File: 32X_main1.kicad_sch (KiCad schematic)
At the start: 27 parts, among them IC504 315-5818, IC505 315-5805, IC509 74AC04

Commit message: Added LCSC Part # for some of the bird seed
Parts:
- C5: LCSC Part # (none) -> C2237864
- C5: LCSC Part # (none) -> C2182015
- FB7: LCSC Part # (none) -> C91037
- R561: LCSC Part # (none) -> C844640
- R562: LCSC Part # (none) -> C2077049
- R566: LCSC Part # (none) -> C2077067
- RM3, RM4, RM5, RM6: LCSC Part # (none) -> C110924
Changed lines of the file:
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@@
+      (effects (font (size 1.27 1.27)) hide)
+    )
+    (property "LCSC Part #" "C2077067" (at 49.53 125.73 0)
       (effects (font (size 1.27 1.27)) hide)
     )
@@
     )
     (property "DigiKey" "" (at 77.47 247.65 0)
+      (effects (font (size 1.27 1.27)) hide)
+    )
+    (property "LCSC Part #" "" (at 77.47 247.65 0)
       (effects (font (size 1.27 1.27)) hide)
     )
@@
       (effects (font (size 1.27 1.27)) hide)
     )
+    (property "LCSC Part #" "C2237864" (at 195.58 243.84 0)
+      (effects (font (size 1.27 1.27)) hide)
+    )
     (pin "1")
     (pin "2")
@@
     )
     (property "DigiKey" "" (at 278.13 244.475 0)
+      (effects (font (size 1.27 1.27)) hide)
+    )
+    (property "LCSC Part #" "" (at 278.13 244.475 0)
       (effects (font (size 1.27 1.27)) hide)
     )
@@
       (effects (font (size 1.27 1.27)) hide)
     )
+    (property "LCSC Part #" "C2237864" (at 194.945 183.515 0)
+      (effects (font (size 1.27 1.27)) hide)
+    )
     (pin "1")
     (pin "2")
@@
     )
     (property "DigiKey" "" (at 85.725 65.405 0)
+      (effects (font (size 1.27 1.27)) hide)
+    )
+    (property "LCSC Part #" "C110924" (at 85.725 65.405 0)
       (effects (font (size 1.27 1.27)) hide)
     )
@@
       (effects (font (size 1.27 1.27)) hide)
     )
+    (property "LCSC Part #" "C2182015" (at 207.645 243.84 0)
+      (effects (font (size 1.27 1.27)) hide)
+    )
     (pin "1")
     (pin "2")
@@
       (effects (font (size 1.27 1.27)) hide)
     )
+    (property "LCSC Part #" "C2182015" (at 291.465 161.29 0)
+      (effects (font (size 1.27 1.27)) hide)
+    )
     (pin "1")
     (pin "2")
@@
       (effects (font (size 1.27 1.27)) hide)
     )
+    (property "LCSC Part #" "C2237864" (at 272.415 161.29 0)
+      (effects (font (size 1.27 1.27)) hide)
+    )
     (pin "1")
     (pin "2")
@@
       (effects (font (size 1.27 1.27)) hide)
     )
+    (property "LCSC Part #" "C2237864" (at 282.575 161.29 0)
+      (effects (font (size 1.27 1.27)) hide)
+    )
     (pin "1")
     (pin "2")
@@
       (effects (font (size 1.27 1.27)) hide)
     )
+    (property "LCSC Part #" "" (at 108.585 198.755 0)
+      (effects (font (size 1.27 1.27)) hide)
+    )
     (pin "1")
     (pin "2")
@@
       (effects (font (size 1.27 1.27)) hide)
     )
+    (property "LCSC Part #" "" (at 263.525 203.2 0)
+      (effects (font (size 1.27 1.27)) hide)
+    )
     (pin "1")
     (pin "2")
@@
       (effects (font (size 1.27 1.27)) hide)
     )
+    (property "LCSC Part #" "" (at 118.11 184.785 0)
+      (effects (font (size 1.27 1.27)) hide)
+    )
     (pin "1")
     (pin "2")
@@
       (effects (font (size 1.27 1.27)) hide)
     )
+    (property "LCSC Part #" "" (at 232.41 243.84 0)
+      (effects (font (size 1.27 1.27)) hide)
+    )
     (pin "1")
     (pin "2")
@@
       (effects (font (size 1.27 1.27)) hide)
     )
+    (property "LCSC Part #" "C91037" (at 236.22 203.2 0)
+      (effects (font (size 1.27 1.27)) hide)
+    )
     (pin "1")
     (pin "2")
@@
       (effects (font (size 1.27 1.27)) hide)
     )
+    (property "LCSC Part #" "C91037" (at 153.67 169.545 0)
+      (effects (font (size 1.27 1.27)) hide)
+    )
     (pin "1")
     (pin "2")
@@
     )
     (property "DigiKey" "" (at 98.425 247.65 0)
+      (effects (font (size 1.27 1.27)) hide)
+    )
+    (property "LCSC Part #" "" (at 98.425 247.65 0)
       (effects (font (size 1.27 1.27)) hide)
     )
@@
       (effects (font (size 1.27 1.27)) hide)
     )
+    (property "LCSC Part #" "C110924" (at 85.725 104.14 0)
+      (effects (font (size 1.27 1.27)) hide)
+    )
     (pin "1")
     (pin "2")
@@
     )
     (property "DigiKey" "" (at 118.11 156.845 0)
+      (effects (font (size 1.27 1.27)) hide)
+    )
+    (property "LCSC Part #" "" (at 118.11 156.845 0)
       (effects (font (size 1.27 1.27)) hide)
     )
@@
       (effects (font (size 1.27 1.27)) hide)
     )
+    (property "LCSC Part #" "C844640" (at 88.265 234.315 0)
+      (effects (font (size 1.27 1.27)) hide)
+    )
     (pin "1")
     (pin "2")
@@
     )
     (property "DigiKey" "" (at 85.725 84.455 0)
+      (effects (font (size 1.27 1.27)) hide)
+    )
+    (property "LCSC Part #" "C110924" (at 85.725 84.455 0)
       (effects (font (size 1.27 1.27)) hide)
     )
@@
       (effects (font (size 1.27 1.27)) hide)
     )
+    (property "LCSC Part #" "C2077049" (at 59.055 247.65 0)
+      (effects (font (size 1.27 1.27)) hide)
+    )
     (pin "1")
     (pin "2")
@@
       (effects (font (size 1.27 1.27)) hide)
     )
+    (property "LCSC Part #" "" (at 203.835 170.815 0)
+      (effects (font (size 1.27 1.27)) hide)
+    )
     (pin "1")
     (pin "2")
@@
     )
     (property "DigiKey" "" (at 220.345 243.84 0)
+      (effects (font (size 1.27 1.27)) hide)
+    )
+    (property "LCSC Part #" "C2182015" (at 220.345 243.84 0)
       (effects (font (size 1.27 1.27)) hide)
     )
@@
     )
     (property "DigiKey" "" (at 249.555 48.26 0)
+      (effects (font (size 1.27 1.27)) hide)
+    )
+    (property "LCSC Part #" "" (at 249.555 48.26 0)
       (effects (font (size 1.27 1.27)) hide)
     )
@@
       (effects (font (size 1.27 1.27)) hide)
     )
+    (property "LCSC Part #" "C2182015" (at 203.835 183.515 0)
+      (effects (font (size 1.27 1.27)) hide)
+    )
     (pin "1")
     (pin "2")
@@
     )
     (property "DigiKey" "" (at 249.555 203.2 0)
+      (effects (font (size 1.27 1.27)) hide)
+    )
+    (property "LCSC Part #" "" (at 249.555 203.2 0)
       (effects (font (size 1.27 1.27)) hide)
     )
@@
       (effects (font (size 1.27 1.27)) hide)
     )
+    (property "LCSC Part #" "" (at 153.67 179.705 0)
+      (effects (font (size 1.27 1.27)) hide)
+    )
     (pin "1")
     (pin "2")
@@
       (effects (font (size 1.27 1.27)) hide)
     )
+    (property "LCSC Part #" "" (at 132.715 156.845 0)
+      (effects (font (size 1.27 1.27)) hide)
+    )
     (pin "1")
     (pin "2")
@@
     )
     (property "DigiKey" "" (at 85.725 123.19 0)
+      (effects (font (size 1.27 1.27)) hide)
+    )
+    (property "LCSC Part #" "C110924" (at 85.725 123.19 0)
       (effects (font (size 1.27 1.27)) hide)
     )
@@
       (effects (font (size 1.27 1.27)) hide)
     )
+    (property "LCSC Part #" "" (at 176.53 48.26 0)
+      (effects (font (size 1.27 1.27)) hide)
+    )

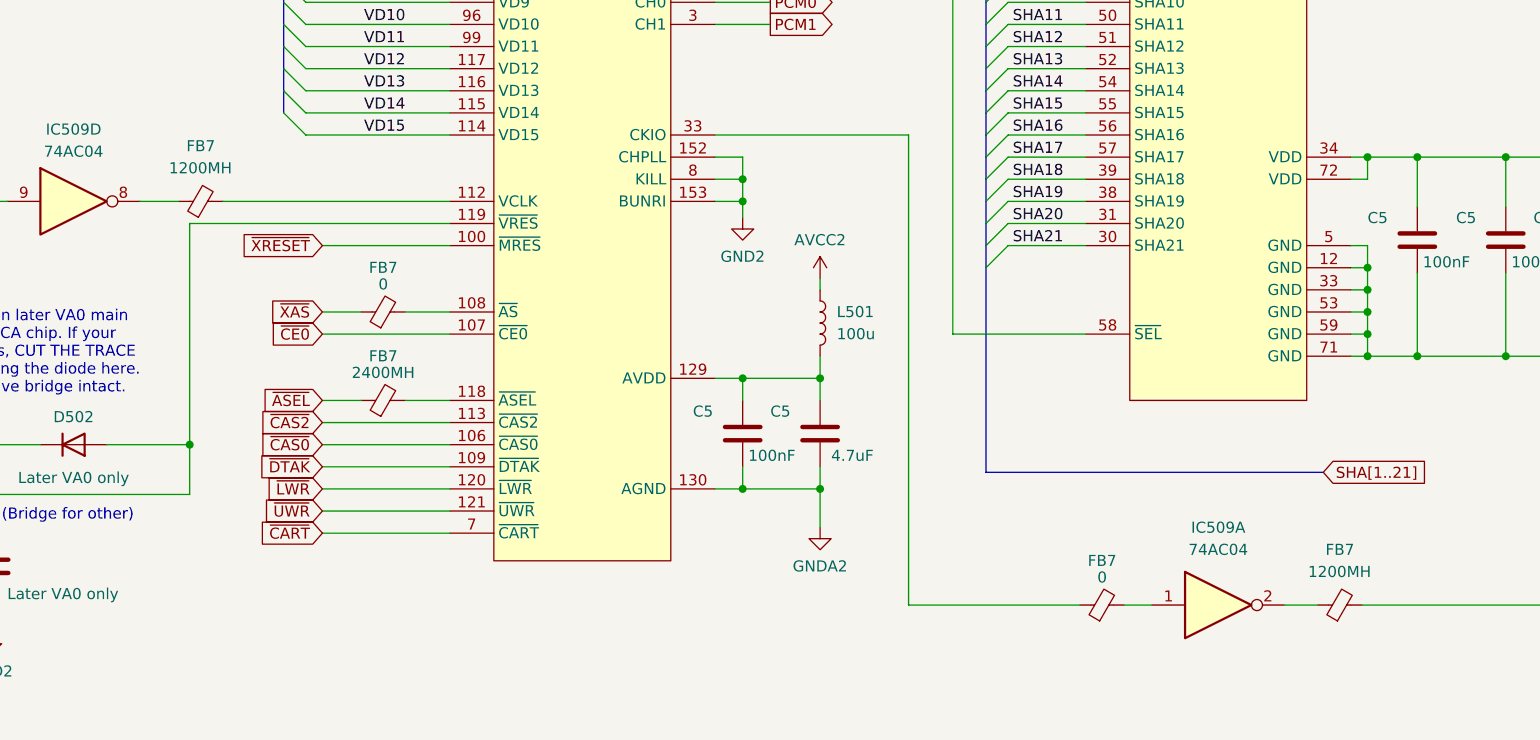
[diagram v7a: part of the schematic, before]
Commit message: Fix FB values.
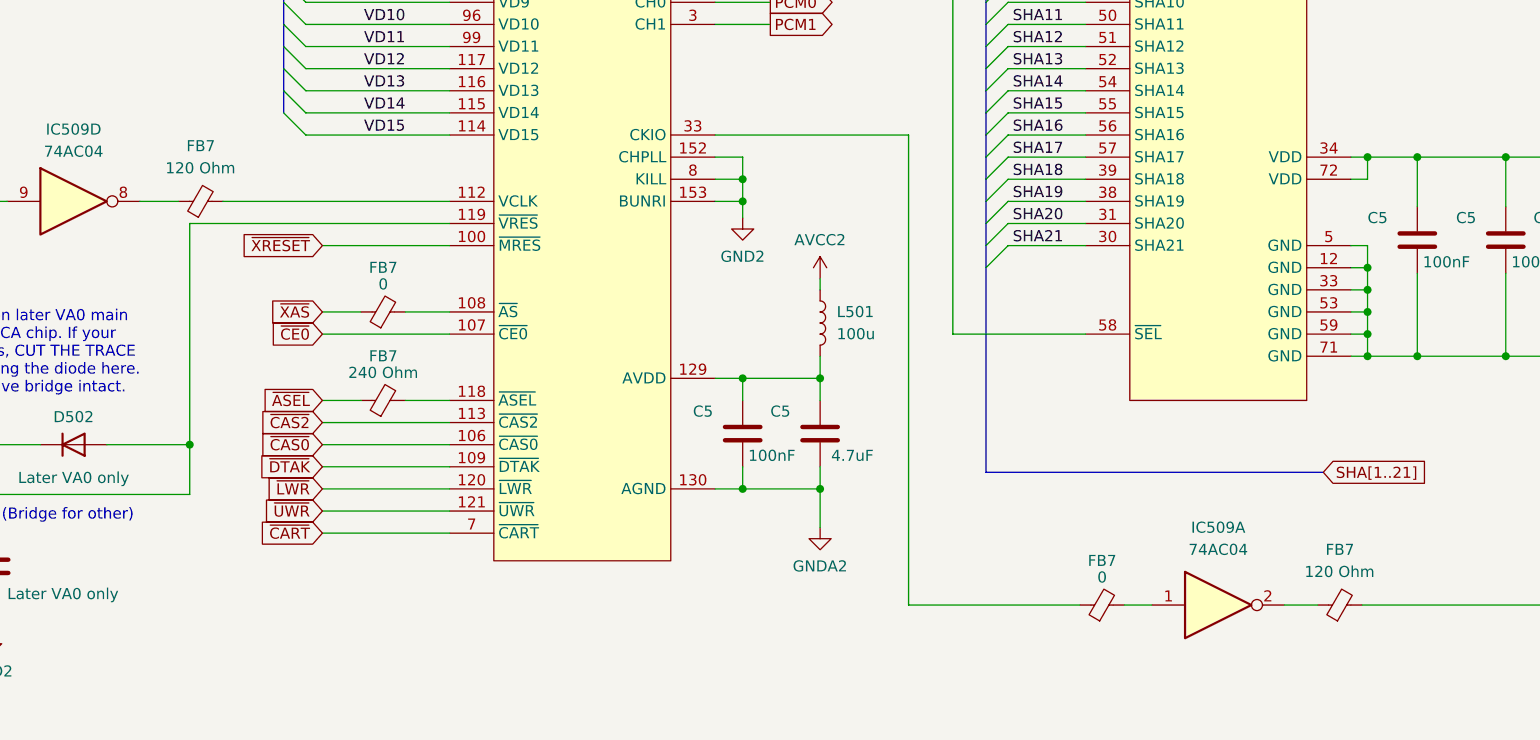
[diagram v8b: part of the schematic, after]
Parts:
- FB7: value 1200MH -> 120 Ohm
- FB7: value 2400MH -> 240 Ohm
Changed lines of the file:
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@@
       (effects (font (size 1.27 1.27)))
     )
-    (property "Value" "1200MH" (at 263.4869 199.39 90)
+    (property "Value" "120 Ohm" (at 263.4869 199.39 90)
       (effects (font (size 1.27 1.27)))
     )
@@
       (effects (font (size 1.27 1.27)))
     )
-    (property "Value" "2400MH" (at 153.67 176.53 90)
+    (property "Value" "240 Ohm" (at 153.67 176.53 90)
       (effects (font (size 1.27 1.27)))
     )
@@
       (effects (font (size 1.27 1.27)))
     )
-    (property "Value" "1200MH" (at 132.6769 153.035 90)
-      (effects (font (size 1.27 1.27)))
-    )
+    (property "Value" "120 Ohm" (at 132.6769 153.035 90)
+      (effects (font (size 1.27 1.27)))
+    )
